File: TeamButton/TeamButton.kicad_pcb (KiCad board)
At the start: 2 copper layers, 79.9 x 70 mm, 5 parts, among them J1 RJ45, SW1 10T85 Microswitch, SW2 10T85 Microswitch

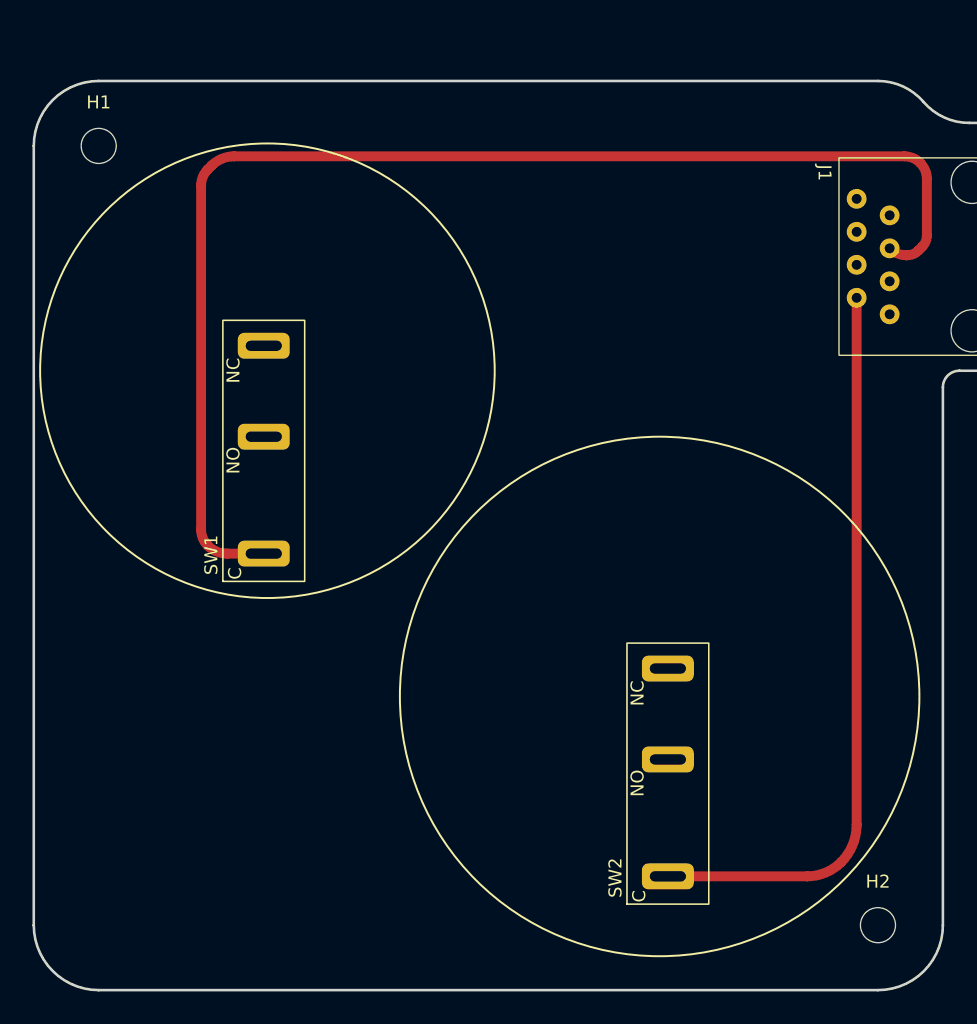
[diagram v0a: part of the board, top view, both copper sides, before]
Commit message: Updated team buttonboard to use M3 fasteners!
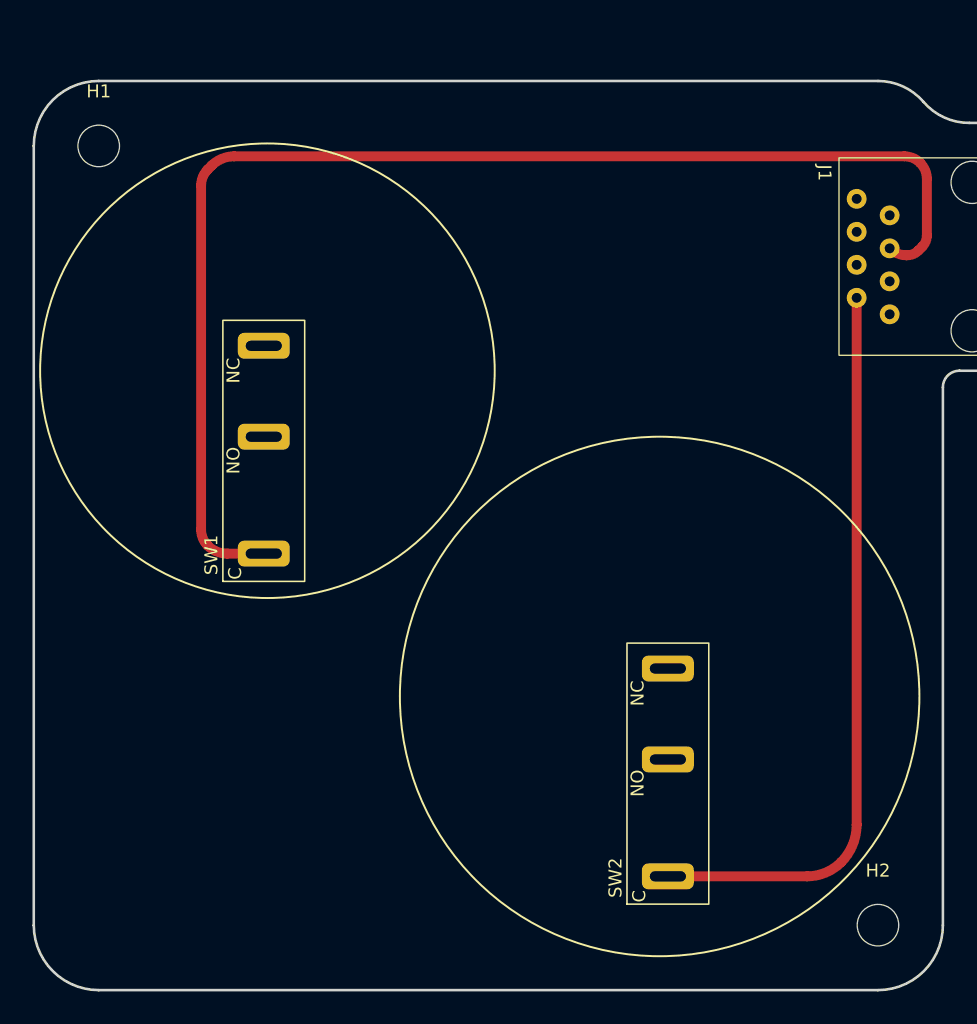
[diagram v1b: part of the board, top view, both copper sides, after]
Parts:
- H1, H2: footprint MountingHole:MountingHole_2.7mm_M2.5_DIN965 -> MountingHole:MountingHole_3.2mm_M3
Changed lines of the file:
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@@
       (net 7 "unconnected-(J1-Pad8)") (pintype "passive"))
   )
-  (footprint "MountingHole:MountingHole_2.7mm_M2.5_DIN965" (layer "F.Cu")
+  (footprint "MountingHole:MountingHole_3.2mm_M3" (layer "F.Cu")
     (at 140 110)
-    (descr "Mounting Hole 2.7mm, no annular, M2.5, DIN965")
-    (tags "mounting hole 2.7mm no annular m2.5 din965")
+    (descr "Mounting Hole 3.2mm, no annular, M3")
+    (tags "mounting hole 3.2mm no annular m3")
     (property "Sheetfile" "TeamButton.kicad_sch")
     (property "Sheetname" "")
     (property "ki_description" "Mounting Hole without connection")
     (property "ki_keywords" "mounting hole")
-    (fp_text reference "H2" (at 0 -3.35) (layer "F.SilkS")
+    (attr exclude_from_pos_files)
+    (fp_text reference "H2" (at 0 -4.2) (layer "F.SilkS")
         (effects (font (size 1 1) (thickness 0.15)))
     )
-    (fp_text value "MountingHole" (at 0 3.35) (layer "F.Fab")
+    (fp_text value "MountingHole" (at 0 4.2) (layer "F.Fab")
         (effects (font (size 1 1) (thickness 0.15)))
     )
@@
         (effects (font (size 1 1) (thickness 0.15)))
     )
-    (fp_circle (center 0 0) (end 2.35 0)
+    (fp_circle (center 0 0) (end 3.2 0)
       (stroke (width 0.15) (type solid)) (fill none) (layer "Cmts.User"))
-    (fp_circle (center 0 0) (end 2.6 0)
+    (fp_circle (center 0 0) (end 3.45 0)
       (stroke (width 0.05) (type solid)) (fill none) (layer "F.CrtYd"))
-    (pad "" np_thru_hole circle (at 0 0) (size 2.7 2.7) (drill 2.7) (layers "*.Cu" "*.Mask"))
+    (pad "" np_thru_hole circle (at 0 0) (size 3.2 3.2) (drill 3.2) (layers "*.Cu" "*.Mask"))
   )
   (footprint "footprints:10T85 Microswitch" (layer "F.Cu")
@@
       (net 1 "GND") (pinfunction "NO") (pintype "passive"))
   )
-  (footprint "MountingHole:MountingHole_2.7mm_M2.5_DIN965" (layer "F.Cu")
+  (footprint "MountingHole:MountingHole_3.2mm_M3" (layer "F.Cu")
     (at 80 50)
-    (descr "Mounting Hole 2.7mm, no annular, M2.5, DIN965")
-    (tags "mounting hole 2.7mm no annular m2.5 din965")
+    (descr "Mounting Hole 3.2mm, no annular, M3")
+    (tags "mounting hole 3.2mm no annular m3")
     (property "Sheetfile" "TeamButton.kicad_sch")
     (property "Sheetname" "")
     (property "ki_description" "Mounting Hole without connection")
     (property "ki_keywords" "mounting hole")
-    (fp_text reference "H1" (at 0 -3.35) (layer "F.SilkS")
+    (attr exclude_from_pos_files)
+    (fp_text reference "H1" (at 0 -4.2) (layer "F.SilkS")
         (effects (font (size 1 1) (thickness 0.15)))
     )
-    (fp_text value "MountingHole" (at 0 3.35) (layer "F.Fab")
+    (fp_text value "MountingHole" (at 0 4.2) (layer "F.Fab")
         (effects (font (size 1 1) (thickness 0.15)))
     )
@@
         (effects (font (size 1 1) (thickness 0.15)))
     )
-    (fp_circle (center 0 0) (end 2.35 0)
+    (fp_circle (center 0 0) (end 3.2 0)
       (stroke (width 0.15) (type solid)) (fill none) (layer "Cmts.User"))
-    (fp_circle (center 0 0) (end 2.6 0)
+    (fp_circle (center 0 0) (end 3.45 0)
       (stroke (width 0.05) (type solid)) (fill none) (layer "F.CrtYd"))
-    (pad "" np_thru_hole circle (at 0 0) (size 2.7 2.7) (drill 2.7) (layers "*.Cu" "*.Mask"))
+    (pad "" np_thru_hole circle (at 0 0) (size 3.2 3.2) (drill 3.2) (layers "*.Cu" "*.Mask"))
   )
   (gr_circle (center 123.19 92.39) (end 143.19 92.39)

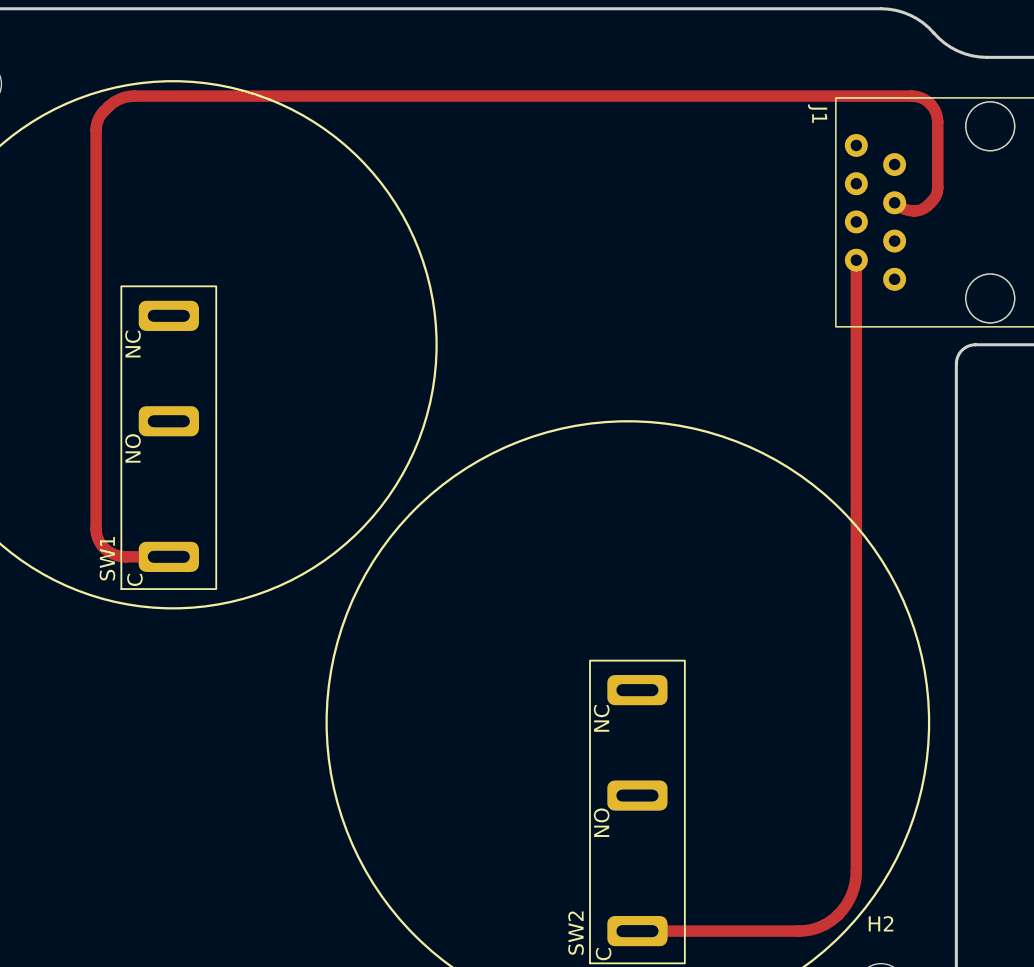
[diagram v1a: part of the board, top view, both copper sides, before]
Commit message: Updated Button and Stacklight PCB to not have backwards fucking footprint shit.
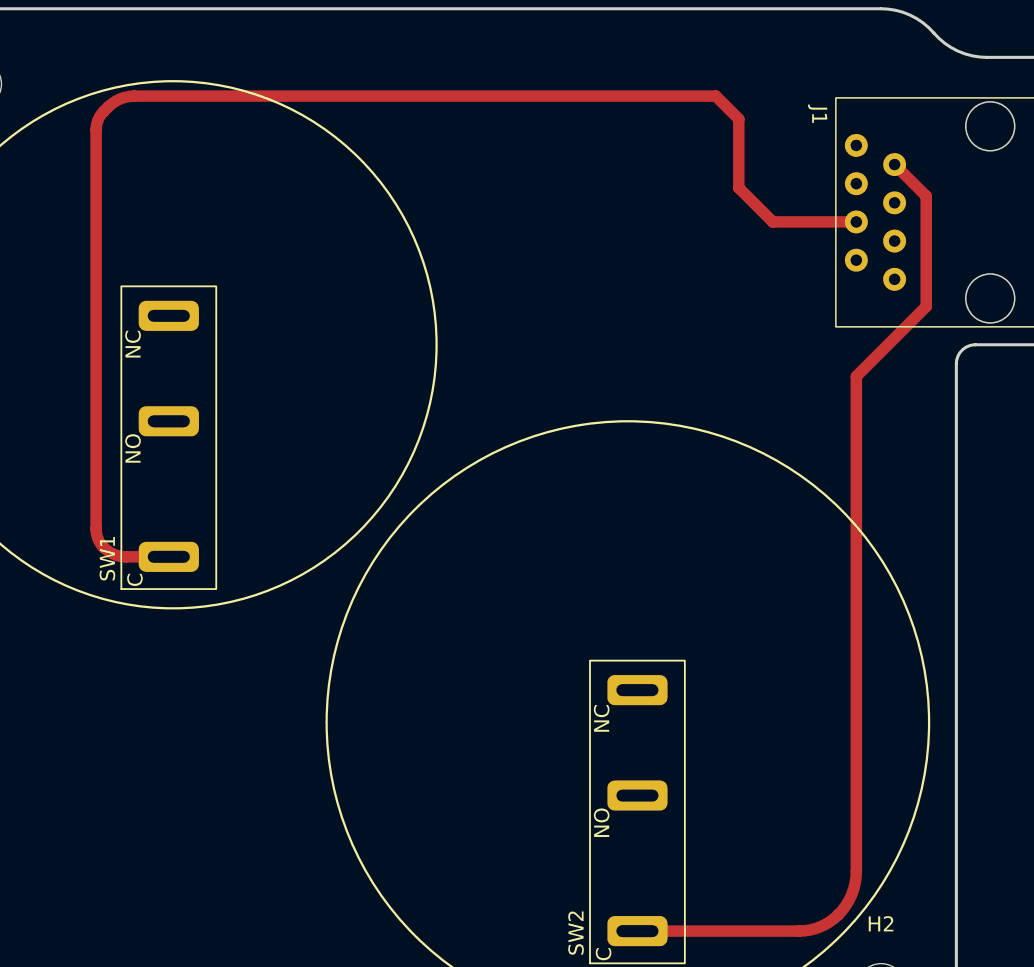
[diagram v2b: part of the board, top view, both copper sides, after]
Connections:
- J1 pad 1: GND -> unconnected-(J1-Pad1)
- J1 pad 2: Net-(SW2-C) -> unconnected-(J1-Pad2)
- J1 pad 4: unconnected-(J1-Pad4) -> Net-(SW1-C)
- J1 pad 5: Net-(SW1-C) -> unconnected-(J1-Pad5)
- J1 pad 7: unconnected-(J1-Pad7) -> Net-(SW2-C)
- J1 pad 8: unconnected-(J1-Pad8) -> GND
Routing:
- net Net-(SW2-C): track 57.4 -> 66.5 mm
- net Net-(SW1-C): track 98.5 -> 90.1 mm
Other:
- board text added: "V2 FLIPPED PAIRS TO WORK W V4 ARENA"
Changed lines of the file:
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@@
   (net 1 "GND")
   (net 2 "unconnected-(J1-Pad3)")
-  (net 3 "unconnected-(J1-Pad4)")
+  (net 3 "unconnected-(J1-Pad1)")
   (net 4 "unconnected-(J1-Pad6)")
-  (net 5 "unconnected-(J1-Pad7)")
+  (net 5 "unconnected-(J1-Pad2)")
   (net 6 "Net-(SW2-C)")
-  (net 7 "unconnected-(J1-Pad8)")
+  (net 7 "unconnected-(J1-Pad5)")
   (net 8 "Net-(SW1-C)")
   (net 9 "unconnected-(SW1-NC-Pad2)")
@@
       (stroke (width 0.1) (type solid)) (fill none) (layer "F.Fab"))
     (pad "1" thru_hole circle (at 12.045 14 270) (size 1.524 1.524) (drill 0.762) (layers "*.Cu" "*.Mask")
-      (net 1 "GND") (pintype "passive"))
+      (net 3 "unconnected-(J1-Pad1)") (pintype "passive"))
     (pad "2" thru_hole circle (at 10.775 16.54 270) (size 1.524 1.524) (drill 0.762) (layers "*.Cu" "*.Mask")
-      (net 6 "Net-(SW2-C)") (pintype "passive"))
+      (net 5 "unconnected-(J1-Pad2)") (pintype "passive"))
     (pad "3" thru_hole circle (at 9.505 14 270) (size 1.524 1.524) (drill 0.762) (layers "*.Cu" "*.Mask")
       (net 2 "unconnected-(J1-Pad3)") (pintype "passive"))
     (pad "4" thru_hole circle (at 8.235 16.54 270) (size 1.524 1.524) (drill 0.762) (layers "*.Cu" "*.Mask")
-      (net 3 "unconnected-(J1-Pad4)") (pintype "passive"))
+      (net 8 "Net-(SW1-C)") (pintype "passive"))
     (pad "5" thru_hole circle (at 6.965 14 270) (size 1.524 1.524) (drill 0.762) (layers "*.Cu" "*.Mask")
-      (net 8 "Net-(SW1-C)") (pintype "passive"))
+      (net 7 "unconnected-(J1-Pad5)") (pintype "passive"))
     (pad "6" thru_hole circle (at 5.695 16.54 270) (size 1.524 1.524) (drill 0.762) (layers "*.Cu" "*.Mask")
       (net 4 "unconnected-(J1-Pad6)") (pintype "passive"))
     (pad "7" thru_hole circle (at 4.425 14 270) (size 1.524 1.524) (drill 0.762) (layers "*.Cu" "*.Mask")
-      (net 5 "unconnected-(J1-Pad7)") (pintype "passive"))
+      (net 6 "Net-(SW2-C)") (pintype "passive"))
     (pad "8" thru_hole circle (at 3.155 16.54 270) (size 1.524 1.524) (drill 0.762) (layers "*.Cu" "*.Mask")
-      (net 7 "unconnected-(J1-Pad8)") (pintype "passive"))
+      (net 1 "GND") (pintype "passive"))
   )
   (footprint "MountingHole:MountingHole_3.2mm_M3" (layer "F.Cu")
@@
   (gr_line (start 65 35) (end 155 35)
     (stroke (width 0.15) (type default)) (layer "User.1"))
+  (gr_text "V2\nFLIPPED PAIRS TO WORK W V4 ARENA" (at 76.962 112.268) (layer "B.SilkS")
+    (effects (font (size 1.5 1.5) (thickness 0.3) bold) (justify left bottom))
+  )
   (gr_text "JLCJLCJLCJLC" (at 152.4 64.008 90) (layer "F.SilkS")
     (effects (font (size 1 1) (thickness 0.15)) (justify left bottom))
@@
   (segment (start 123.825 97.24) (end 123.825 96.52) (width 0.25) (layer "F.Cu") (net 1))
   (segment (start 134.542993 106.24) (end 123.825 106.24) (width 0.762) (layer "F.Cu") (net 6))
-  (segment (start 138.36 61.695) (end 138.36 102.258944) (width 0.762) (layer "F.Cu") (net 6))
+  (segment (start 140.9 55.345) (end 143.002 57.447) (width 0.762) (layer "F.Cu") (net 6))
+  (segment (start 143.002 57.447) (end 143.002 64.77) (width 0.762) (layer "F.Cu") (net 6))
+  (segment (start 138.36 69.412) (end 138.36 102.258944) (width 0.762) (layer "F.Cu") (net 6))
+  (segment (start 143.002 64.77) (end 138.36 69.412) (width 0.762) (layer "F.Cu") (net 6))
   (arc (start 138.36 102.258944) (mid 138.04813 103.826819) (end 137.16 105.156) (width 0.762) (layer "F.Cu") (net 6))
   (arc (start 137.16 105.156) (mid 135.959307 105.958278) (end 134.542993 106.24) (width 0.762) (layer "F.Cu") (net 6))
-  (segment (start 143.764 56.896) (end 143.764 52.53442) (width 0.762) (layer "F.Cu") (net 8))
-  (segment (start 143.107211 58.060789) (end 143.40479 57.76321) (width 0.762) (layer "F.Cu") (net 8))
-  (segment (start 87.884 53.04242) (end 87.884 79.54558) (width 0.762) (layer "F.Cu") (net 8))
-  (segment (start 89.883983 81.39) (end 92.71 81.39) (width 0.762) (layer "F.Cu") (net 8))
-  (segment (start 142.02958 50.8) (end 90.424 50.8) (width 0.762) (layer "F.Cu") (net 8))
-  (segment (start 88.689579 51.518421) (end 88.392 51.816) (width 0.762) (layer "F.Cu") (net 8))
-  (segment (start 142.191604 58.42) (end 142.24 58.42) (width 0.762) (layer "F.Cu") (net 8))
-  (arc (start 90.424 50.8) (mid 89.485338 50.986712) (end 88.689579 51.518421) (width 0.762) (layer "F.Cu") (net 8))
-  (arc (start 87.884 79.54558) (mid 88.016024 80.209313) (end 88.392 80.772) (width 0.762) (layer "F.Cu") (net 8))
-  (arc (start 142.24 58.42) (mid 142.709332 58.326644) (end 143.107211 58.060789) (width 0.762) (layer "F.Cu") (net 8))
-  (arc (start 88.392 51.816) (mid 88.016025 52.378687) (end 87.884 53.04242) (width 0.762) (layer "F.Cu") (net 8))
-  (arc (start 143.764 52.53442) (mid 143.631975 51.870686) (end 143.256 51.308) (width 0.762) (layer "F.Cu") (net 8))
-  (arc (start 143.256 51.308) (mid 142.693314 50.932025) (end 142.02958 50.8) (width 0.762) (layer "F.Cu") (net 8))
-  (arc (start 143.40479 57.76321) (mid 143.670644 57.365331) (end 143.764 56.896) (width 0.762) (layer "F.Cu") (net 8))
-  (arc (start 88.392 80.772) (mid 89.076527 81.229387) (end 89.883983 81.39) (width 0.762) (layer "F.Cu") (net 8))
-  (arc (start 140.9 57.885) (mid 141.492593 58.280958) (end 142.191604 58.42) (width 0.762) (layer "F.Cu") (net 8))
+  (segment (start 130.556 56.896) (end 132.815 59.155) (width 0.762) (layer "F.Cu") (net 8))
+  (segment (start 132.815 59.155) (end 138.36 59.155) (width 0.762) (layer "F.Cu") (net 8))
+  (segment (start 129.032 50.8) (end 130.556 52.324) (width 0.762) (layer "F.Cu") (net 8))
+  (segment (start 92.71 81.39) (end 89.883983 81.39) (width 0.762) (layer "F.Cu") (net 8))
+  (segment (start 88.392 51.816) (end 88.689579 51.518421) (width 0.762) (layer "F.Cu") (net 8))
+  (segment (start 90.424 50.8) (end 129.032 50.8) (width 0.762) (layer "F.Cu") (net 8))
+  (segment (start 87.884 79.54558) (end 87.884 53.04242) (width 0.762) (layer "F.Cu") (net 8))
+  (segment (start 130.556 52.324) (end 130.556 56.896) (width 0.762) (layer "F.Cu") (net 8))
+  (arc (start 88.689579 51.518421) (mid 89.485338 50.986712) (end 90.424 50.8) (width 0.762) (layer "F.Cu") (net 8))
+  (arc (start 88.392 80.772) (mid 88.016024 80.209313) (end 87.884 79.54558) (width 0.762) (layer "F.Cu") (net 8))
+  (arc (start 87.884 53.04242) (mid 88.016025 52.378687) (end 88.392 51.816) (width 0.762) (layer "F.Cu") (net 8))
+  (arc (start 89.883983 81.39) (mid 89.076527 81.229387) (end 88.392 80.772) (width 0.762) (layer "F.Cu") (net 8))
   (zone (net 1) (net_name "GND") (layers "F&B.Cu") (name "GND") (hatch edge 0.508)
     (connect_pads (clearance 0.508))
